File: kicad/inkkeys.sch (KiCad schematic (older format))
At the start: 38 parts, among them SW1 Rotary_Encoder_Switch, SW2 SW_Push

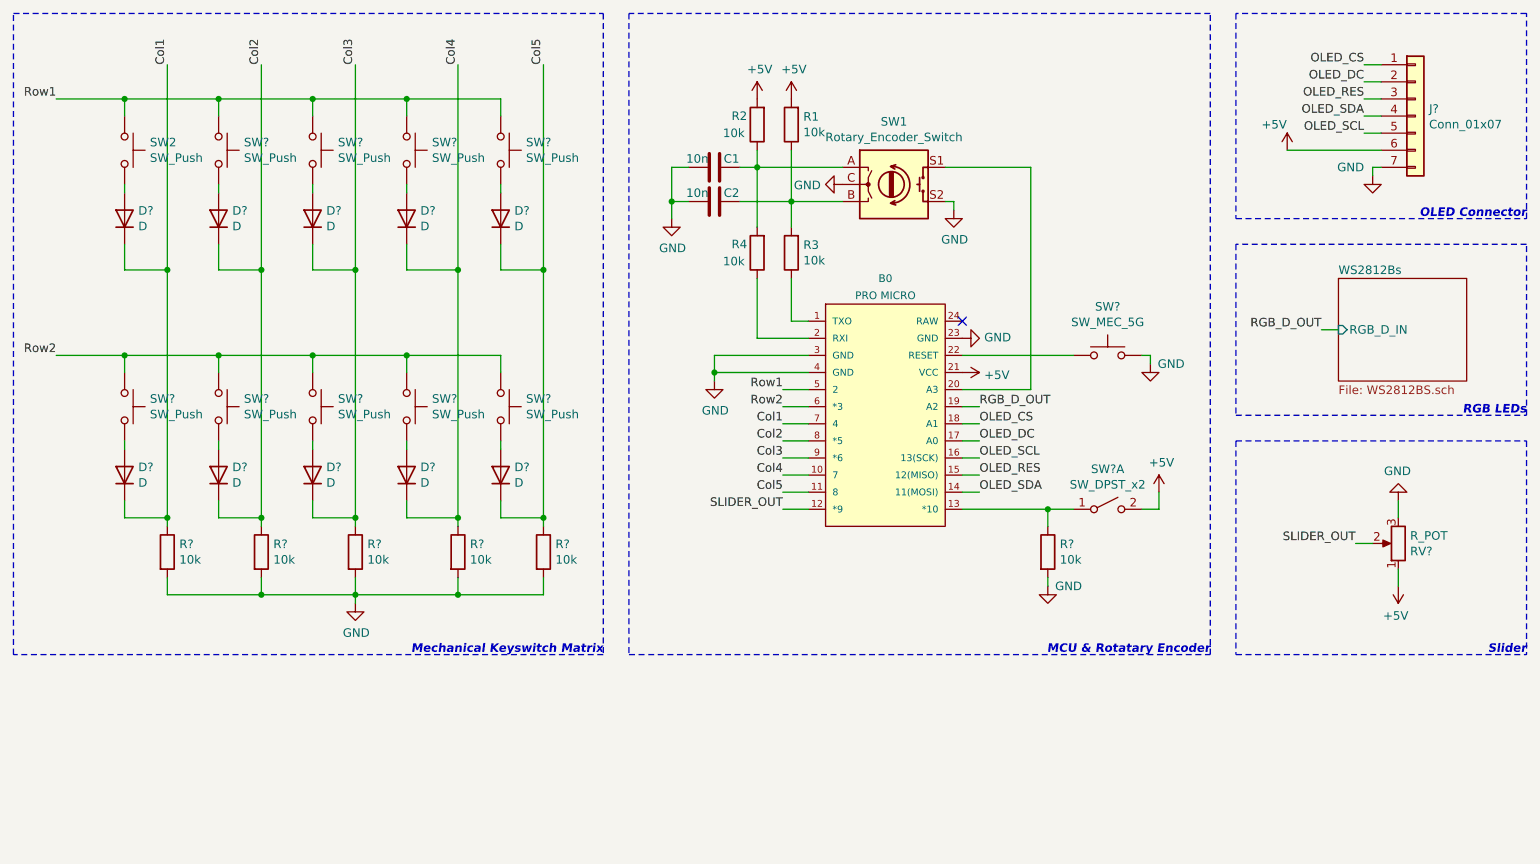
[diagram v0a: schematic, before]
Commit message: Updated labels and added footprints
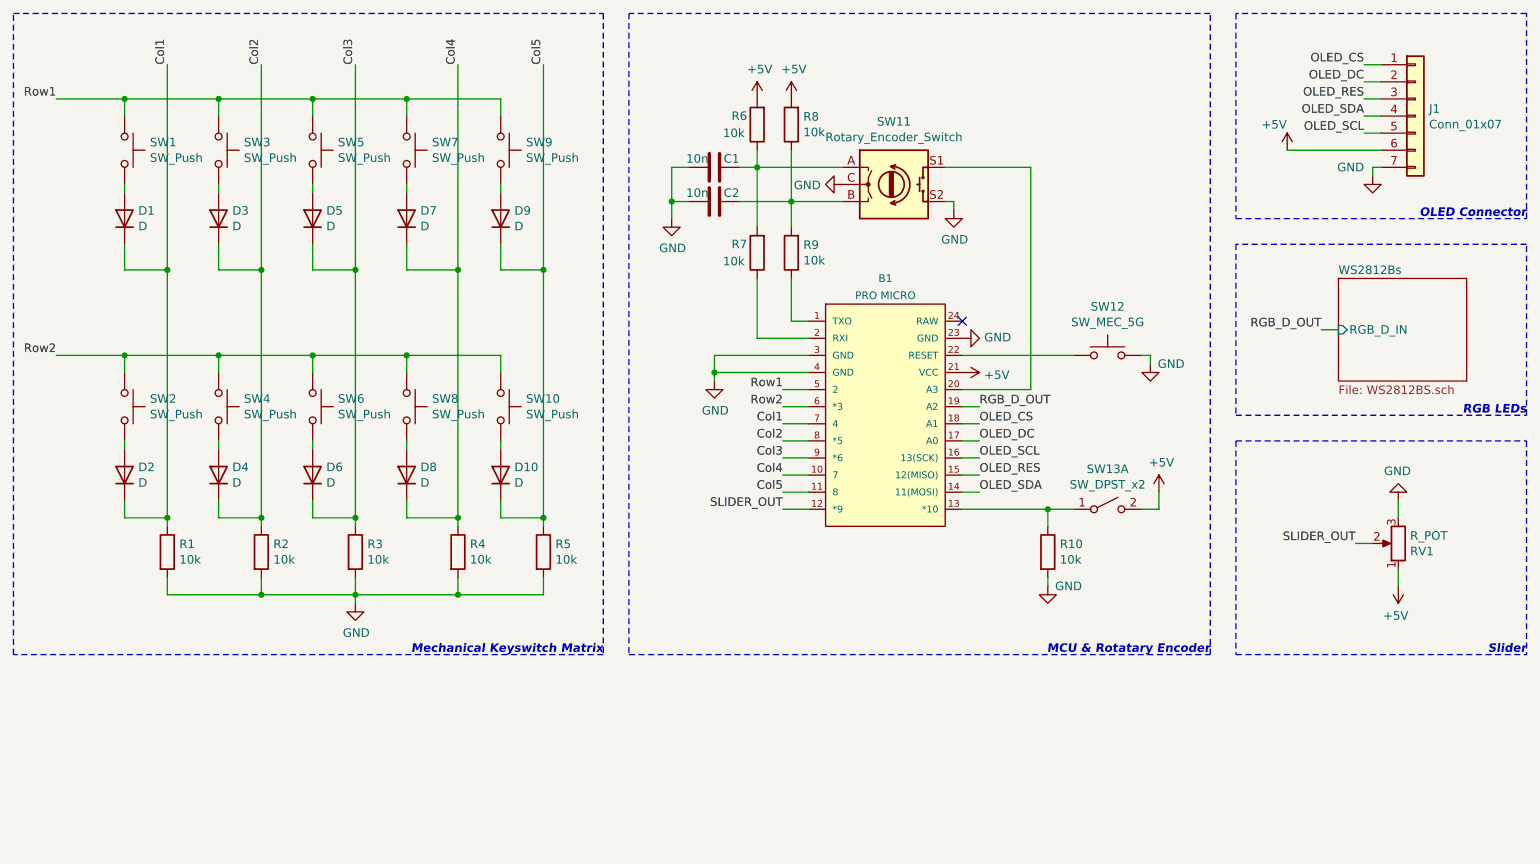
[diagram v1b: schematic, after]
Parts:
- D1, D10, D2, D3, D4, D5, D6, D7, D8, D9: renamed from D?; footprint (none) -> Diode_SMD:D_1206_3216Metric_Pad1.42x1.75mm_HandSolder
- J1: renamed from J?; footprint (none) -> Connector_PinHeader_2.54mm:PinHeader_1x07_P2.54mm_Horizontal
- R1, R10, R2, R3, R4, R5: renamed from R?; footprint (none) -> Resistor_SMD:R_1206_3216Metric_Pad1.30x1.75mm_HandSolder
- R6: renamed from R2; footprint Resistor_THT:R_Axial_DIN0207_L6.3mm_D2.5mm_P10.16mm_Horizontal -> Resistor_SMD:R_1206_3216Metric_Pad1.30x1.75mm_HandSolder
- R7: renamed from R4; footprint Resistor_THT:R_Axial_DIN0207_L6.3mm_D2.5mm_P10.16mm_Horizontal -> Resistor_SMD:R_1206_3216Metric_Pad1.30x1.75mm_HandSolder
- R8: renamed from R1; footprint Resistor_THT:R_Axial_DIN0207_L6.3mm_D2.5mm_P10.16mm_Horizontal -> Resistor_SMD:R_1206_3216Metric_Pad1.30x1.75mm_HandSolder
- R9: renamed from R3; footprint Resistor_THT:R_Axial_DIN0207_L6.3mm_D2.5mm_P10.16mm_Horizontal -> Resistor_SMD:R_1206_3216Metric_Pad1.30x1.75mm_HandSolder
- RV1: renamed from RV?; footprint (none) -> Connector_PinHeader_2.54mm:PinHeader_1x03_P2.54mm_Horizontal
- SW12: renamed from SW?; footprint (none) -> Button_Switch_THT:SW_PUSH_6mm_H5mm
- SW13: renamed from SW?; footprint (none) -> Connector_PinHeader_2.54mm:PinHeader_1x02_P2.54mm_Horizontal
- gave numbers to parts that had none: 9
- renumbered B0 to B1, SW2 to SW1, SW1 to SW11

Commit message: PCB Layout started
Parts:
- added H1, H2, H3, H4: MountingHole, MountingHole:MountingHole_3.2mm_M3, symbol Mechanical:MountingHole
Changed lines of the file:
@@
 Text Notes 9600 2200 2    50   Italic 10
 OLED Connector
+$Comp
+L Mechanical:MountingHole H1
+U 1 1 609FF5C5
+P 7950 5250
+F 0 "H1" H 8050 5296 50  0000 L CNN
+F 1 "MountingHole" H 8050 5205 50  0000 L CNN
+F 2 "MountingHole:MountingHole_3.2mm_M3" H 7950 5250 50  0001 C CNN
+F 3 "~" H 7950 5250 50  0001 C CNN
+	1    7950 5250
+	1    0    0    -1
+$EndComp
+$Comp
+L Mechanical:MountingHole H3
+U 1 1 609FFBDC
+P 8800 5250
+F 0 "H3" H 8900 5296 50  0000 L CNN
+F 1 "MountingHole" H 8900 5205 50  0000 L CNN
+F 2 "MountingHole:MountingHole_3.2mm_M3" H 8800 5250 50  0001 C CNN
+F 3 "~" H 8800 5250 50  0001 C CNN
+	1    8800 5250
+	1    0    0    -1
+$EndComp
+$Comp
+L Mechanical:MountingHole H2
+U 1 1 609FFE7B
+P 7950 5800
+F 0 "H2" H 8050 5846 50  0000 L CNN
+F 1 "MountingHole" H 8050 5755 50  0000 L CNN
+F 2 "MountingHole:MountingHole_3.2mm_M3" H 7950 5800 50  0001 C CNN
+F 3 "~" H 7950 5800 50  0001 C CNN
+	1    7950 5800
+	1    0    0    -1
+$EndComp
+$Comp
+L Mechanical:MountingHole H4
+U 1 1 60A0010E
+P 8850 5800
+F 0 "H4" H 8950 5846 50  0000 L CNN
+F 1 "MountingHole" H 8950 5755 50  0000 L CNN
+F 2 "MountingHole:MountingHole_3.2mm_M3" H 8850 5800 50  0001 C CNN
+F 3 "~" H 8850 5800 50  0001 C CNN
+	1    8850 5800
+	1    0    0    -1
+$EndComp
 $EndSCHEMATC

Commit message: PCB Work
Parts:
- removed SW11: Rotary_Encoder_Switch, Rotary_Encoder:RotaryEncoder_Alps_EC11E-Switch_Vertical_H20mm, symbol Device:Rotary_Encoder_Switch
- added J2: Conn_01x05, Connector_PinHeader_2.54mm:PinHeader_1x05_P2.54mm_Horizontal, symbol Connector_Generic:Conn_01x05
- C1, C2: footprint Capacitor_THT:C_Disc_D5.0mm_W2.5mm_P5.00mm -> Capacitor_SMD:C_1206_3216Metric_Pad1.33x1.80mm_HandSolder
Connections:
- net GND: now also J2.2 (Pin_2), J2.5 (Pin_5)
- net RS1: now reaches B1.20 (A3)
- net RS1: now also J2.4 (Pin_4)
- net RA: now reaches C1.1, R6.1, R7.2
- net RA: now also J2.1 (Pin_1)
- net RC: now reaches C2.1, R8.1, R9.2
- net RC: now also J2.3 (Pin_3)
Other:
- note added: "Rotary Encoder"
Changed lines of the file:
@@
 $EndComp
 $Comp
-L Device:Rotary_Encoder_Switch SW11
-U 1 1 5FE26615
-P 5900 2000
-F 0 "SW11" H 5900 2367 50  0000 C CNN
-F 1 "Rotary_Encoder_Switch" H 5900 2276 50  0000 C CNN
-F 2 "Rotary_Encoder:RotaryEncoder_Alps_EC11E-Switch_Vertical_H20mm" H 5750 2160 50  0001 C CNN
-F 3 "~" H 5900 2260 50  0001 C CNN
-	1    5900 2000
-	1    0    0    -1
-$EndComp
-$Comp
 L power:+5V #PWR09
 U 1 1 5FE2A9B7
@@
 F 0 "C1" V 4800 2000 50  0000 C CNN
 F 1 "10n" V 4800 1800 50  0000 C CNN
-F 2 "Capacitor_THT:C_Disc_D5.0mm_W2.5mm_P5.00mm" H 4888 1750 50  0001 C CNN
+F 2 "Capacitor_SMD:C_1206_3216Metric_Pad1.33x1.80mm_HandSolder" H 4888 1750 50  0001 C CNN
 F 3 "~" H 4850 1900 50  0001 C CNN
 	1    4850 1900
@@
 F 0 "C2" V 4800 2200 50  0000 C CNN
 F 1 "10n" V 4800 2000 50  0000 C CNN
-F 2 "Capacitor_THT:C_Disc_D5.0mm_W2.5mm_P5.00mm" H 4888 1950 50  0001 C CNN
+F 2 "Capacitor_SMD:C_1206_3216Metric_Pad1.33x1.80mm_HandSolder" H 4888 1950 50  0001 C CNN
 F 3 "~" H 4850 2100 50  0001 C CNN
 	1    4850 2100
@@
 	1    0    0    -1
 $EndComp
+$Comp
+L Connector_Generic:Conn_01x05 J2
+U 1 1 60A1BEF4
+P 6000 1150
+F 0 "J2" V 5964 862 50  0000 R CNN
+F 1 "Conn_01x05" V 5873 862 50  0000 R CNN
+F 2 "Connector_PinHeader_2.54mm:PinHeader_1x05_P2.54mm_Horizontal" H 6000 1150 50  0001 C CNN
+F 3 "~" H 6000 1150 50  0001 C CNN
+	1    6000 1150
+	0    -1   -1   0
+$EndComp
+Text Label 5600 1900 0    50   ~ 0
+RA
+Text Label 5900 1400 3    50   ~ 0
+RB
+Text Label 6000 1400 3    50   ~ 0
+RC
+Text Label 6100 1400 3    50   ~ 0
+RS1
+Text Label 6200 1400 3    50   ~ 0
+RS2
+Wire Wire Line
+	5800 1400 5800 1350
+Wire Wire Line
+	5900 1400 5900 1350
+Wire Wire Line
+	6000 1400 6000 1350
+Wire Wire Line
+	6100 1400 6100 1350
+Wire Wire Line
+	6200 1400 6200 1350
+Text Label 5800 1400 3    50   ~ 0
+RA
+Text Label 5600 2000 0    50   ~ 0
+RB
+Text Label 5600 2100 0    50   ~ 0
+RC
+Text Label 6200 1900 2    50   ~ 0
+RS1
+Text Label 6200 2100 2    50   ~ 0
+RS2
+Wire Notes Line
+	5550 1750 5550 2150
+Wire Notes Line
+	5550 2150 6300 2150
+Wire Notes Line
+	6300 2150 6300 1750
+Wire Notes Line
+	6300 1750 5550 1750
+Text Notes 5550 1750 0    50   ~ 0
+Rotary Encoder
 $EndSCHEMATC

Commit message: Finished PCB and Generated Gerbers
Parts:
- removed SW12: SW_MEC_5G, Button_Switch_THT:SW_PUSH_6mm_H5mm, symbol Switch:SW_MEC_5G
- added SW12: SW_Push, Button_Switch_THT:SW_PUSH_6mm_H5mm, symbol Switch:SW_Push
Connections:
- net GND: now also SW12.2
- net at B1.22 (RESET): now also SW12.1
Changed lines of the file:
@@
 EndData
 $EndBitmap
-$Comp
-L Switch:SW_MEC_5G SW12
-U 1 1 60A0A159
-P 7150 3000
-F 0 "SW12" H 7150 3285 50  0000 C CNN
-F 1 "SW_MEC_5G" H 7150 3194 50  0000 C CNN
-F 2 "Button_Switch_THT:SW_PUSH_6mm_H5mm" H 7150 3200 50  0001 C CNN
-F 3 "http://www.apem.com/int/index.php?controller=attachment&id_attachment=488" H 7150 3200 50  0001 C CNN
-	1    7150 3000
-	1    0    0    -1
-$EndComp
 Wire Wire Line
 	7400 3050 7400 3000
@@
 Text Notes 5550 1750 0    50   ~ 0
 Rotary Encoder
+$Comp
+L Switch:SW_Push SW12
+U 1 1 60B8E746
+P 7150 3000
+F 0 "SW12" H 7150 3285 50  0000 C CNN
+F 1 "SW_Push" H 7150 3194 50  0000 C CNN
+F 2 "Button_Switch_THT:SW_PUSH_6mm_H5mm" H 7150 3200 50  0001 C CNN
+F 3 "~" H 7150 3200 50  0001 C CNN
+	1    7150 3000
+	1    0    0    -1
+$EndComp
 $EndSCHEMATC
